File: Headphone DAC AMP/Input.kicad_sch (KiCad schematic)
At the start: 38 parts, among them J1 2137160001, J4 PINHD_1x2_Male, U2 XU316-1024-QF60B-C24, U8 W25Q16JVSNIQ

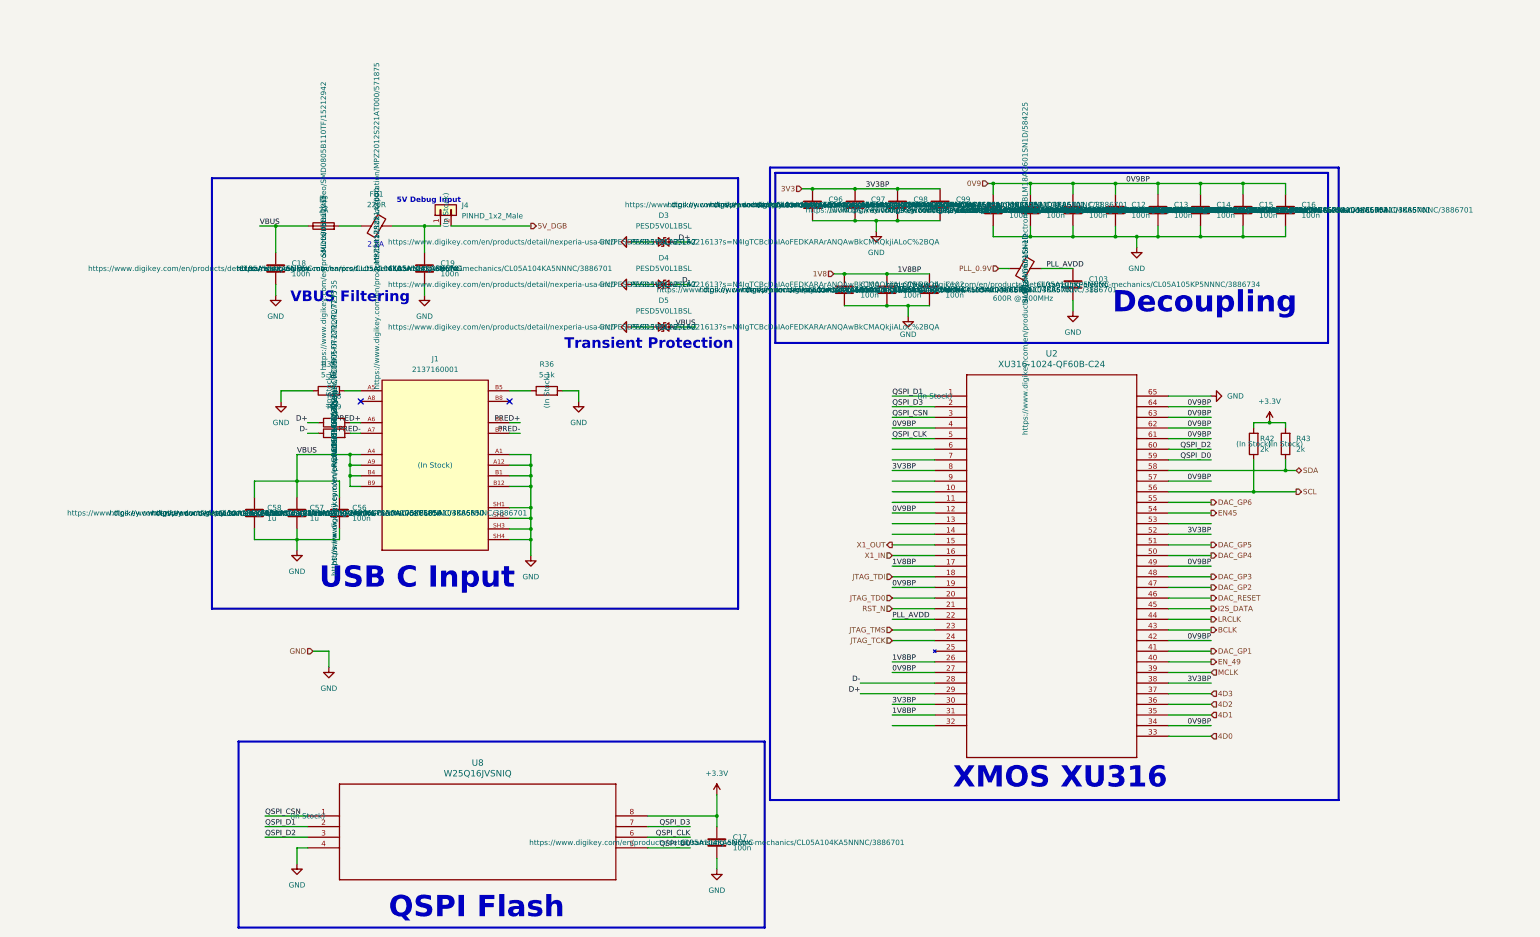
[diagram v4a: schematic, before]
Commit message: Update capacitor footprints
Changed several capacitor footprints in schematic files from 0402/hand-solder variants to standard 0603_1608Metric. Updated PCB with new net and additional property fields for components.
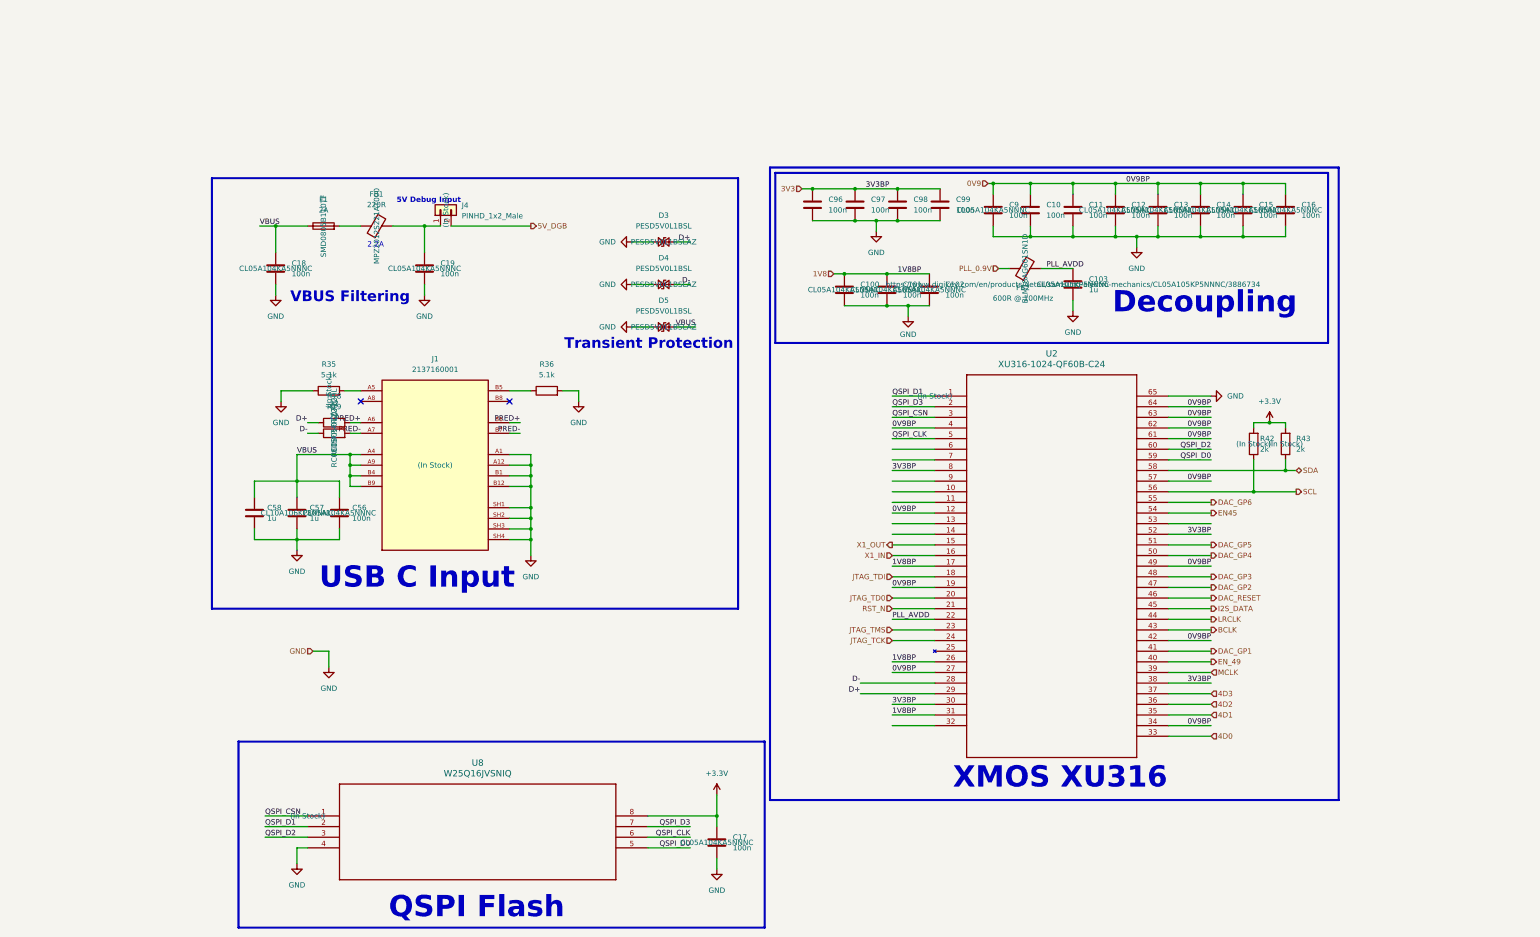
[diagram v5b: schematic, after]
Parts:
- C10, C100, C101, C102, C103, C11, C12, C13, C14, C15, C16, C17, C18, C19, C56, C9, C96, C97, C98, C99: footprint Capacitor_SMD:C_0402_1005Metric_Pad0.74x0.62mm_HandSolder -> Capacitor_SMD:C_0603_1608Metric
- C57, C58: footprint Capacitor_SMD:C_0603_1608Metric_Pad1.08x0.95mm_HandSolder -> Capacitor_SMD:C_0603_1608Metric
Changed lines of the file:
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@@
 					(size 1.27 1.27)
 				)
+				(hide yes)
 			)
 		)
@@
 			)
 		)
-		(property "Footprint" "Capacitor_SMD:C_0402_1005Metric_Pad0.74x0.62mm_HandSolder"
+		(property "Footprint" "Capacitor_SMD:C_0603_1608Metric"
 			(at 65.7352 40.64 0)
 			(effects
@@
 					(size 1.27 1.27)
 				)
+				(hide yes)
 			)
 		)
@@
 			)
 		)
-		(property "Footprint" "Capacitor_SMD:C_0402_1005Metric_Pad0.74x0.62mm_HandSolder"
+		(property "Footprint" "Capacitor_SMD:C_0603_1608Metric"
 			(at 188.9252 25.4 0)
 			(effects
@@
 					(size 1.27 1.27)
 				)
+				(hide yes)
 			)
 		)
@@
 					(size 1.27 1.27)
 				)
+				(hide yes)
 			)
 		)
@@
 					(size 1.27 1.27)
 				)
+				(hide yes)
 			)
 		)
@@
 			)
 		)
-		(property "Footprint" "Capacitor_SMD:C_0402_1005Metric_Pad0.74x0.62mm_HandSolder"
+		(property "Footprint" "Capacitor_SMD:C_0603_1608Metric"
 			(at 230.8352 26.67 0)
 			(effects
@@
 					(size 1.27 1.27)
 				)
+				(hide yes)
 			)
 		)
@@
 					(size 1.27 1.27)
 				)
+				(hide yes)
 			)
 		)
@@
 			)
 		)
-		(property "Footprint" "Capacitor_SMD:C_0402_1005Metric_Pad0.74x0.62mm_HandSolder"
+		(property "Footprint" "Capacitor_SMD:C_0603_1608Metric"
 			(at 166.0652 45.72 0)
 			(effects
@@
 					(size 1.27 1.27)
 				)
+				(hide yes)
 			)
 		)
@@
 			)
 		)
-		(property "Footprint" "Capacitor_SMD:C_0402_1005Metric_Pad0.74x0.62mm_HandSolder"
+		(property "Footprint" "Capacitor_SMD:C_0603_1608Metric"
 			(at 45.4152 99.06 0)
 			(effects
@@
 					(size 1.27 1.27)
 				)
+				(hide yes)
 			)
 		)
@@
 			)
 		)
-		(property "Footprint" "Capacitor_SMD:C_0402_1005Metric_Pad0.74x0.62mm_HandSolder"
+		(property "Footprint" "Capacitor_SMD:C_0603_1608Metric"
 			(at 201.6252 26.67 0)
 			(effects
@@
 					(size 1.27 1.27)
 				)
+				(hide yes)
 			)
 		)
@@
 			)
 		)
-		(property "Footprint" "Capacitor_SMD:C_0402_1005Metric_Pad0.74x0.62mm_HandSolder"
+		(property "Footprint" "Capacitor_SMD:C_0603_1608Metric"
 			(at 186.3852 45.72 0)
 			(effects
@@
 					(size 1.27 1.27)
 				)
+				(hide yes)
 			)
 		)
@@
 			)
 		)
-		(property "Footprint" "Capacitor_SMD:C_0402_1005Metric_Pad0.74x0.62mm_HandSolder"
+		(property "Footprint" "Capacitor_SMD:C_0603_1608Metric"
 			(at 240.9952 26.67 0)
 			(effects
@@
 					(size 1.27 1.27)
 				)
+				(hide yes)
 			)
 		)
@@
 					(size 1.27 1.27)
 				)
+				(hide yes)
 			)
 		)
@@
 					(size 1.27 1.27)
 				)
+				(hide yes)
 			)
 		)
@@
 			)
 		)
-		(property "Footprint" "Capacitor_SMD:C_0402_1005Metric_Pad0.74x0.62mm_HandSolder"
+		(property "Footprint" "Capacitor_SMD:C_0603_1608Metric"
 			(at 168.6052 25.4 0)
 			(effects
@@
 					(size 1.27 1.27)
 				)
+				(hide yes)
 			)
 		)
@@
 					(size 1.27 1.27)
 				)
+				(hide yes)
 			)
 		)
@@
 			)
 		)
-		(property "Footprint" "Capacitor_SMD:C_0402_1005Metric_Pad0.74x0.62mm_HandSolder"
+		(property "Footprint" "Capacitor_SMD:C_0603_1608Metric"
 			(at 30.1752 40.64 0)
 			(effects
@@
 					(size 1.27 1.27)
 				)
+				(hide yes)
 			)
 		)
@@
 			)
 		)
-		(property "Footprint" "Capacitor_SMD:C_0402_1005Metric_Pad0.74x0.62mm_HandSolder"
+		(property "Footprint" "Capacitor_SMD:C_0603_1608Metric"
 			(at 176.2252 45.72 0)
 			(effects
@@
 					(size 1.27 1.27)
 				)
+				(hide yes)
 			)
 		)
@@
 					(size 1.27 1.27)
 				)
+				(hide yes)
 			)
 		)
@@
 					(size 1.27 1.27)
 				)
+				(hide yes)
 			)
 		)
@@
 			)
 		)
-		(property "Footprint" "Capacitor_SMD:C_0402_1005Metric_Pad0.74x0.62mm_HandSolder"
+		(property "Footprint" "Capacitor_SMD:C_0603_1608Metric"
 			(at 271.4752 26.67 0)
 			(effects
@@
 					(size 1.27 1.27)
 				)
+				(hide yes)
 			)
 		)
@@
 			)
 		)
-		(property "Footprint" "Capacitor_SMD:C_0402_1005Metric_Pad0.74x0.62mm_HandSolder"
+		(property "Footprint" "Capacitor_SMD:C_0603_1608Metric"
 			(at 178.7652 25.4 0)
 			(effects
@@
 					(size 1.27 1.27)
 				)
+				(hide yes)
 			)
 		)
@@
 					(size 1.27 1.27)
 				)
+				(hide yes)
 			)
 		)
@@
 			)
 		)
-		(property "Footprint" "Capacitor_SMD:C_0603_1608Metric_Pad1.08x0.95mm_HandSolder"
+		(property "Footprint" "Capacitor_SMD:C_0603_1608Metric"
 			(at 35.2552 99.06 0)
 			(effects
@@
 					(size 1.27 1.27)
 				)
+				(hide yes)
 			)
 		)
@@
 			)
 		)
-		(property "Footprint" "Capacitor_SMD:C_0402_1005Metric_Pad0.74x0.62mm_HandSolder"
+		(property "Footprint" "Capacitor_SMD:C_0603_1608Metric"
 			(at 210.5152 26.67 0)
 			(effects
@@
 					(size 1.27 1.27)
 				)
+				(hide yes)
 			)
 		)
@@
 					(size 1.27 1.27)
 				)
+				(hide yes)
 			)
 		)
@@
 			)
 		)
-		(property "Footprint" "Capacitor_SMD:C_0402_1005Metric_Pad0.74x0.62mm_HandSolder"
+		(property "Footprint" "Capacitor_SMD:C_0603_1608Metric"
 			(at 251.1552 26.67 0)
 			(effects
@@
 					(size 1.27 1.27)
 				)
+				(hide yes)
 			)
 		)
@@
 			)
 		)
-		(property "Footprint" "Capacitor_SMD:C_0402_1005Metric_Pad0.74x0.62mm_HandSolder"
+		(property "Footprint" "Capacitor_SMD:C_0603_1608Metric"
 			(at 220.6752 44.45 0)
 			(effects
@@
 			)
 		)
-		(property "Footprint" "Capacitor_SMD:C_0402_1005Metric_Pad0.74x0.62mm_HandSolder"
+		(property "Footprint" "Capacitor_SMD:C_0603_1608Metric"
 			(at 158.4452 25.4 0)
 			(effects
@@
 					(size 1.27 1.27)
 				)
+				(hide yes)
 			)
 		)
@@
 					(size 1.27 1.27)
 				)
+				(hide yes)
 			)
 		)
@@
 					(size 1.27 1.27)
 				)
+				(hide yes)
 			)
 		)
@@
 			)
 		)
-		(property "Footprint" "Capacitor_SMD:C_0402_1005Metric_Pad0.74x0.62mm_HandSolder"
+		(property "Footprint" "Capacitor_SMD:C_0603_1608Metric"
 			(at 220.6752 26.67 0)
 			(effects
@@
 					(size 1.27 1.27)
 				)
+				(hide yes)
 			)
 		)
@@
 					(size 1.27 1.27)
 				)
+				(hide yes)
 			)
 		)
@@
 					(size 1.27 1.27)
 				)
+				(hide yes)
 			)
 		)
@@
 			)
 		)
-		(property "Footprint" "Capacitor_SMD:C_0402_1005Metric_Pad0.74x0.62mm_HandSolder"
+		(property "Footprint" "Capacitor_SMD:C_0603_1608Metric"
 			(at 135.5852 177.8 0)
 			(effects
@@
 					(size 1.27 1.27)
 				)
+				(hide yes)
 			)
 		)
@@
 			)
 		)
-		(property "Footprint" "Capacitor_SMD:C_0402_1005Metric_Pad0.74x0.62mm_HandSolder"
+		(property "Footprint" "Capacitor_SMD:C_0603_1608Metric"
 			(at 261.3152 26.67 0)
 			(effects
@@
 					(size 1.27 1.27)
 				)
+				(hide yes)
 			)
 		)
@@
 			)
 		)
-		(property "Footprint" "Capacitor_SMD:C_0603_1608Metric_Pad1.08x0.95mm_HandSolder"
+		(property "Footprint" "Capacitor_SMD:C_0603_1608Metric"
 			(at 25.0952 99.06 0)
 			(effects
@@
 					(size 1.27 1.27)
 				)
+				(hide yes)
 			)
 		)
@@
 					(size 1.27 1.27)
 				)
+				(hide yes)
 			)
 		)

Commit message: Worked on power schematic
planning to add debugging options
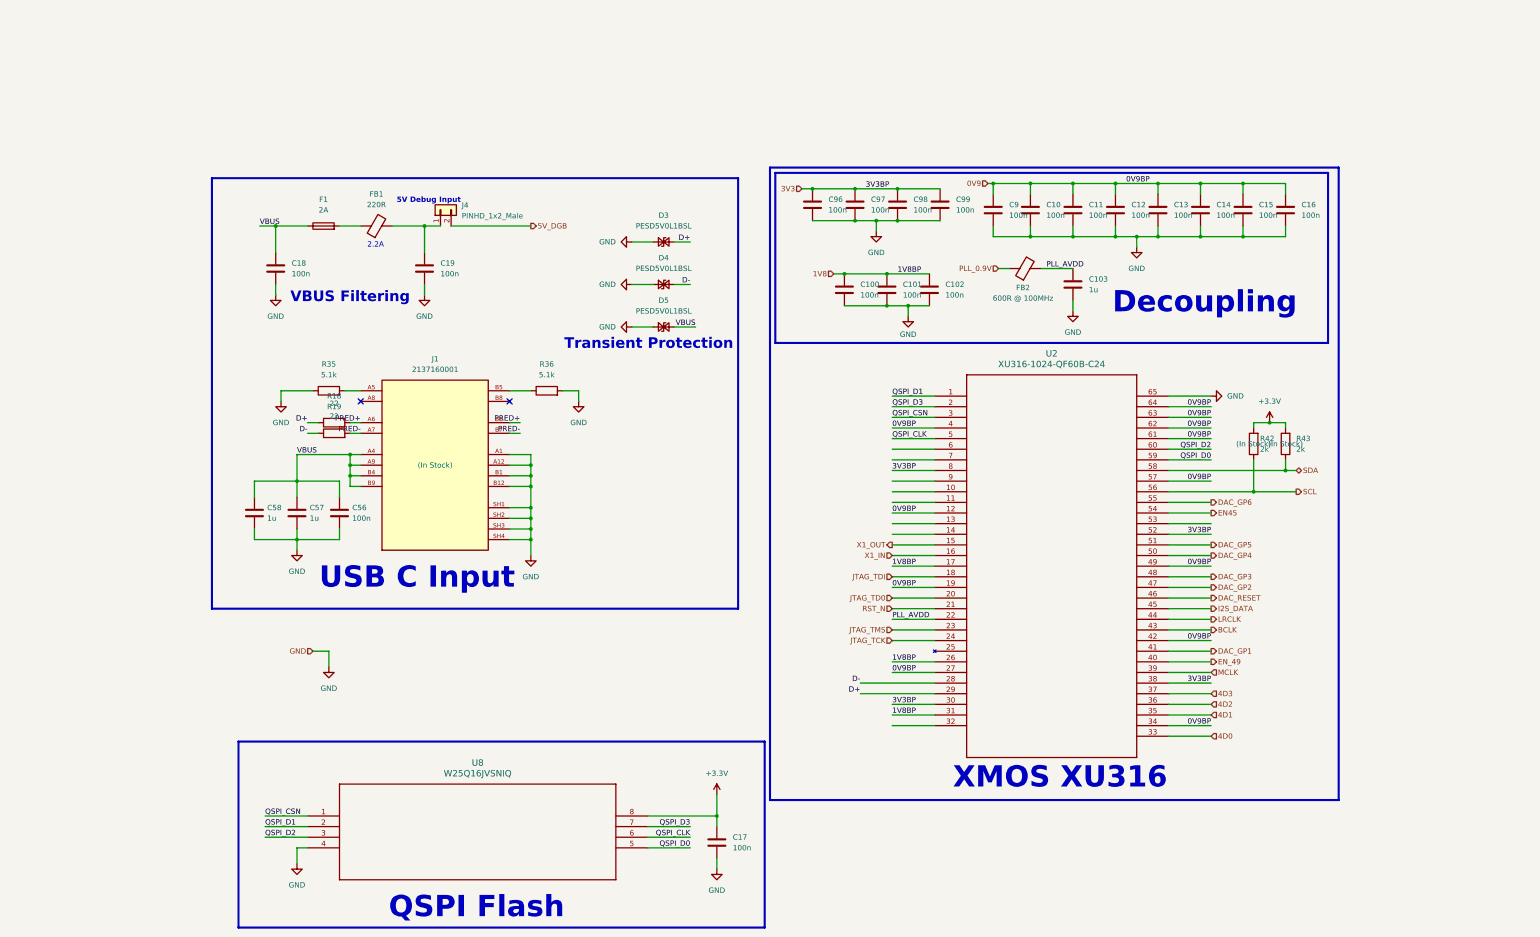
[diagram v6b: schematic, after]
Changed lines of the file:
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@@
 					(size 1.27 1.27)
 				)
+				(hide yes)
 			)
 		)
@@
 					(size 1.27 1.27)
 				)
+				(hide yes)
 			)
 		)
@@
 					(size 1.27 1.27)
 				)
+				(hide yes)
 			)
 		)
@@
 					(size 1.27 1.27)
 				)
+				(hide yes)
 			)
 		)
@@
 					(size 1.27 1.27)
 				)
+				(hide yes)
 			)
 		)
@@
 					(size 1.27 1.27)
 				)
+				(hide yes)
 			)
 		)
@@
 					(size 1.27 1.27)
 				)
+				(hide yes)
 			)
 		)
@@
 					(size 1.27 1.27)
 				)
+				(hide yes)
 			)
 		)
@@
 					(size 1.27 1.27)
 				)
+				(hide yes)
 			)
 		)
@@
 					(size 1.27 1.27)
 				)
+				(hide yes)
 			)
 		)
@@
 					(size 1.27 1.27)
 				)
+				(hide yes)
 			)
 		)
@@
 					(size 1.27 1.27)
 				)
+				(hide yes)
 			)
 		)
@@
 					(size 1.27 1.27)
 				)
+				(hide yes)
 			)
 		)
@@
 					(size 1.27 1.27)
 				)
+				(hide yes)
 			)
 		)
@@
 					(size 1.27 1.27)
 				)
+				(hide yes)
 			)
 		)
@@
 					(size 1.27 1.27)
 				)
+				(hide yes)
 			)
 		)
@@
 					(size 1.27 1.27)
 				)
+				(hide yes)
 			)
 		)
@@
 					(size 1.27 1.27)
 				)
+				(hide yes)
 			)
 		)
@@
 					(size 1.27 1.27)
 				)
+				(hide yes)
 			)
 		)
@@
 					(size 1.27 1.27)
 				)
+				(hide yes)
 			)
 		)
@@
 					(size 1.27 1.27)
 				)
+				(hide yes)
 			)
 		)
@@
 					(size 1.27 1.27)
 				)
+				(hide yes)
 			)
 		)
@@
 					(size 1.27 1.27)
 				)
+				(hide yes)
 			)
 		)
@@
 					(size 1.27 1.27)
 				)
+				(hide yes)
 			)
 		)
@@
 					(size 1.27 1.27)
 				)
+				(hide yes)
 			)
 		)
@@
 					(size 1.27 1.27)
 				)
+				(hide yes)
 			)
 		)
@@
 					(size 1.27 1.27)
 				)
+				(hide yes)
 			)
 		)
@@
 					(size 1.27 1.27)
 				)
+				(hide yes)
 			)
 		)

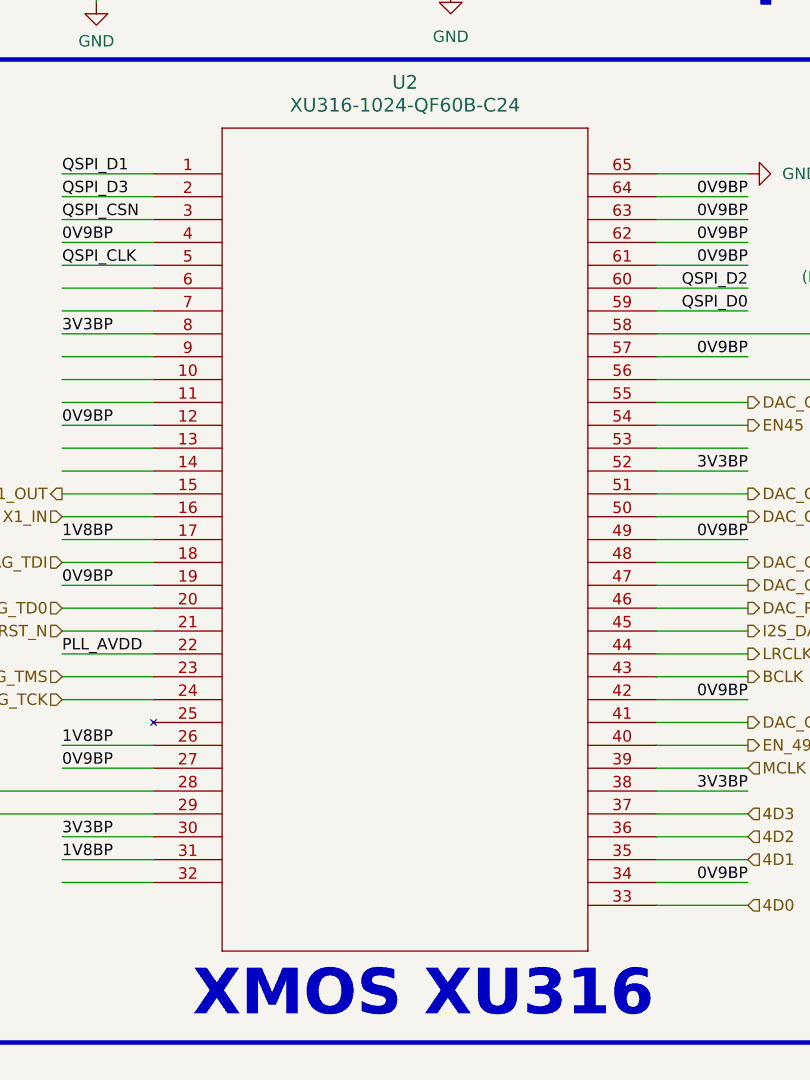
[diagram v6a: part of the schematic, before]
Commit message: Added 0.9V regulator footprint
There is still an issue where the nets are not being populated correctly across the schematic to PCB view
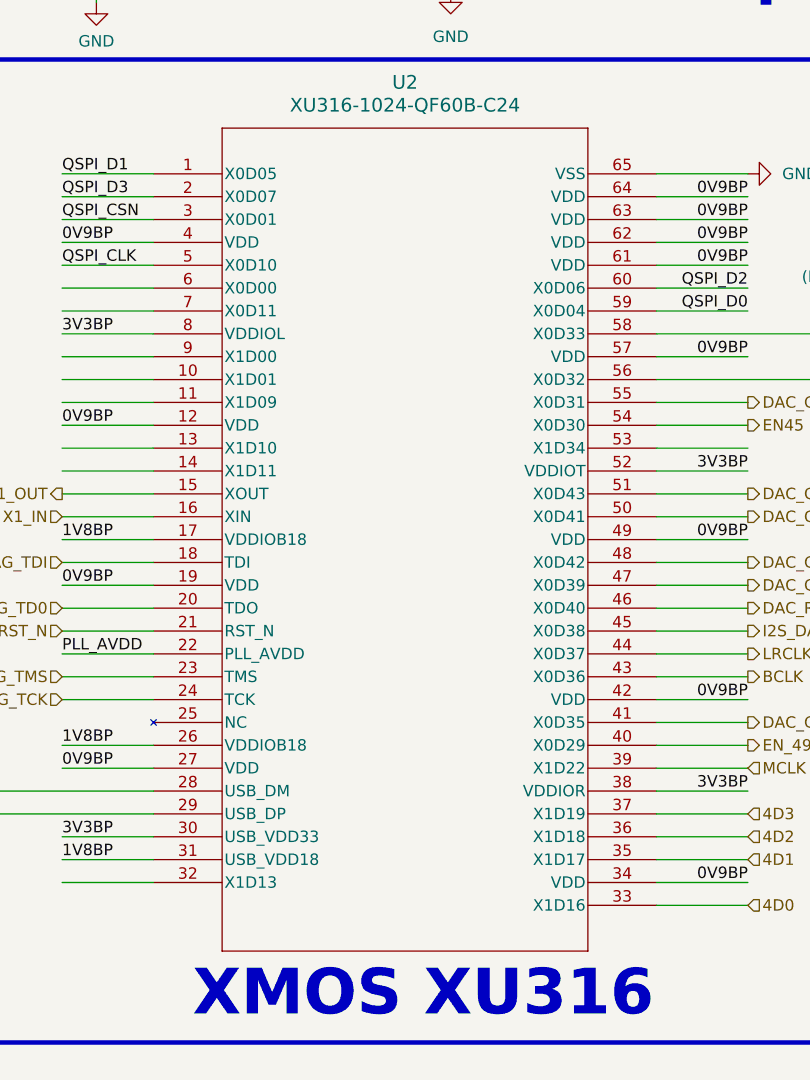
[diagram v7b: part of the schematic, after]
